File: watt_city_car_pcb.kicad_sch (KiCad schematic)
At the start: 0 parts

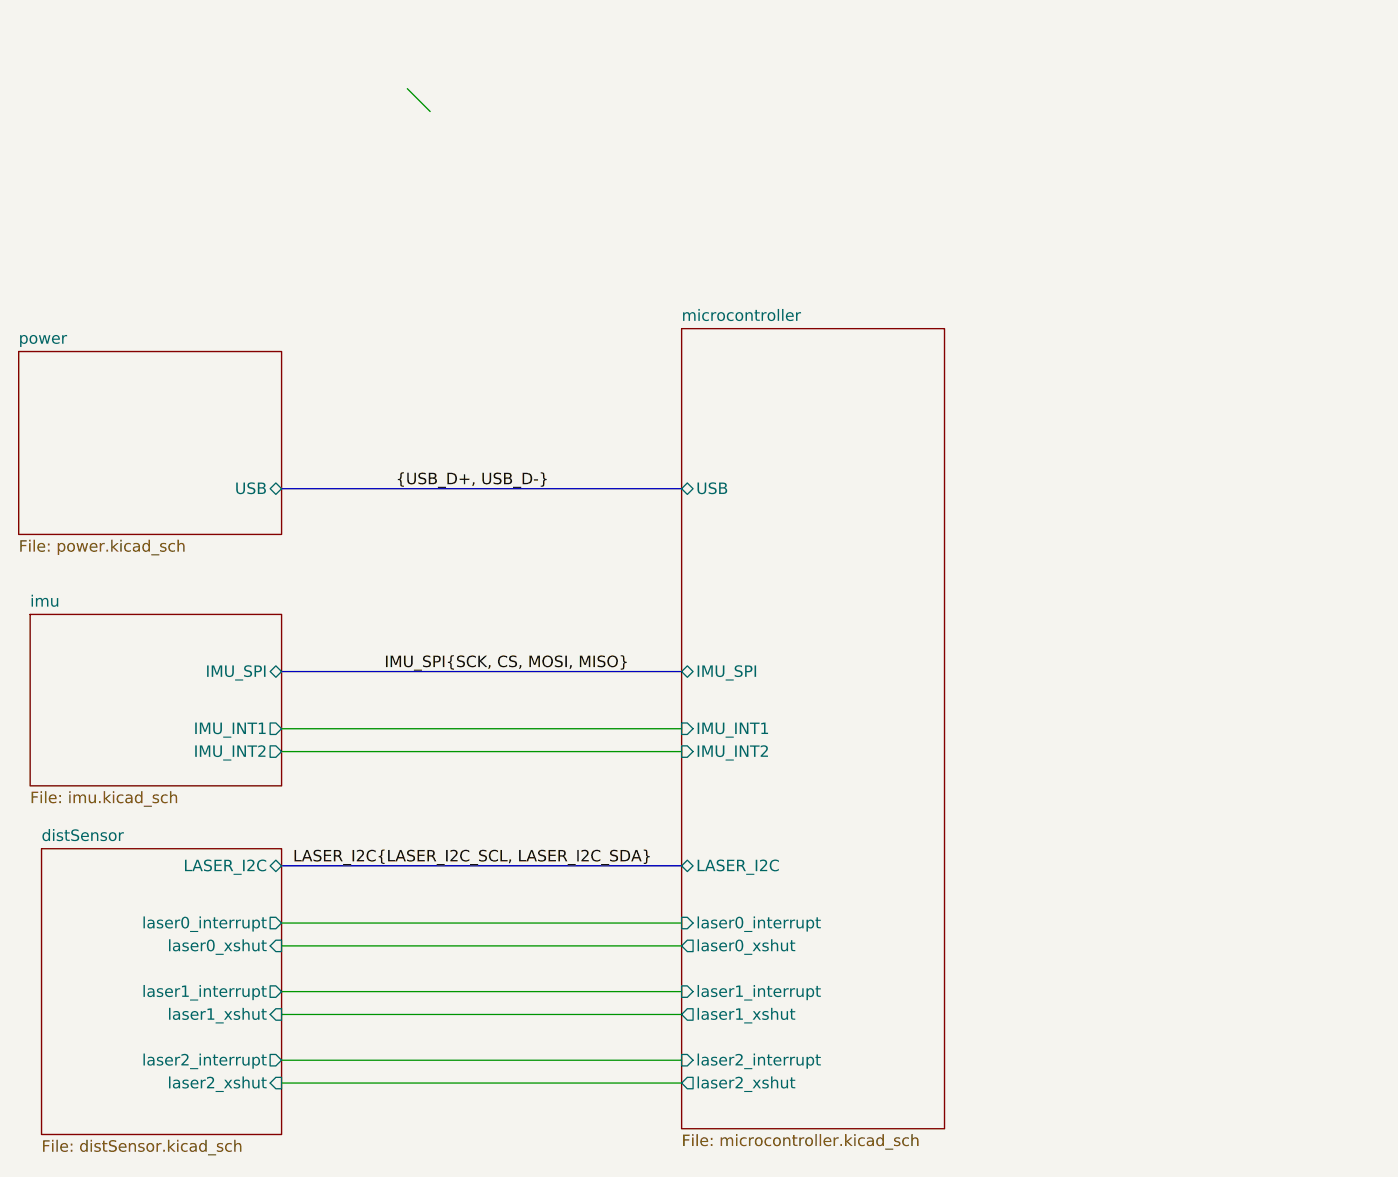
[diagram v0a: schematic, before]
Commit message: added motor controller
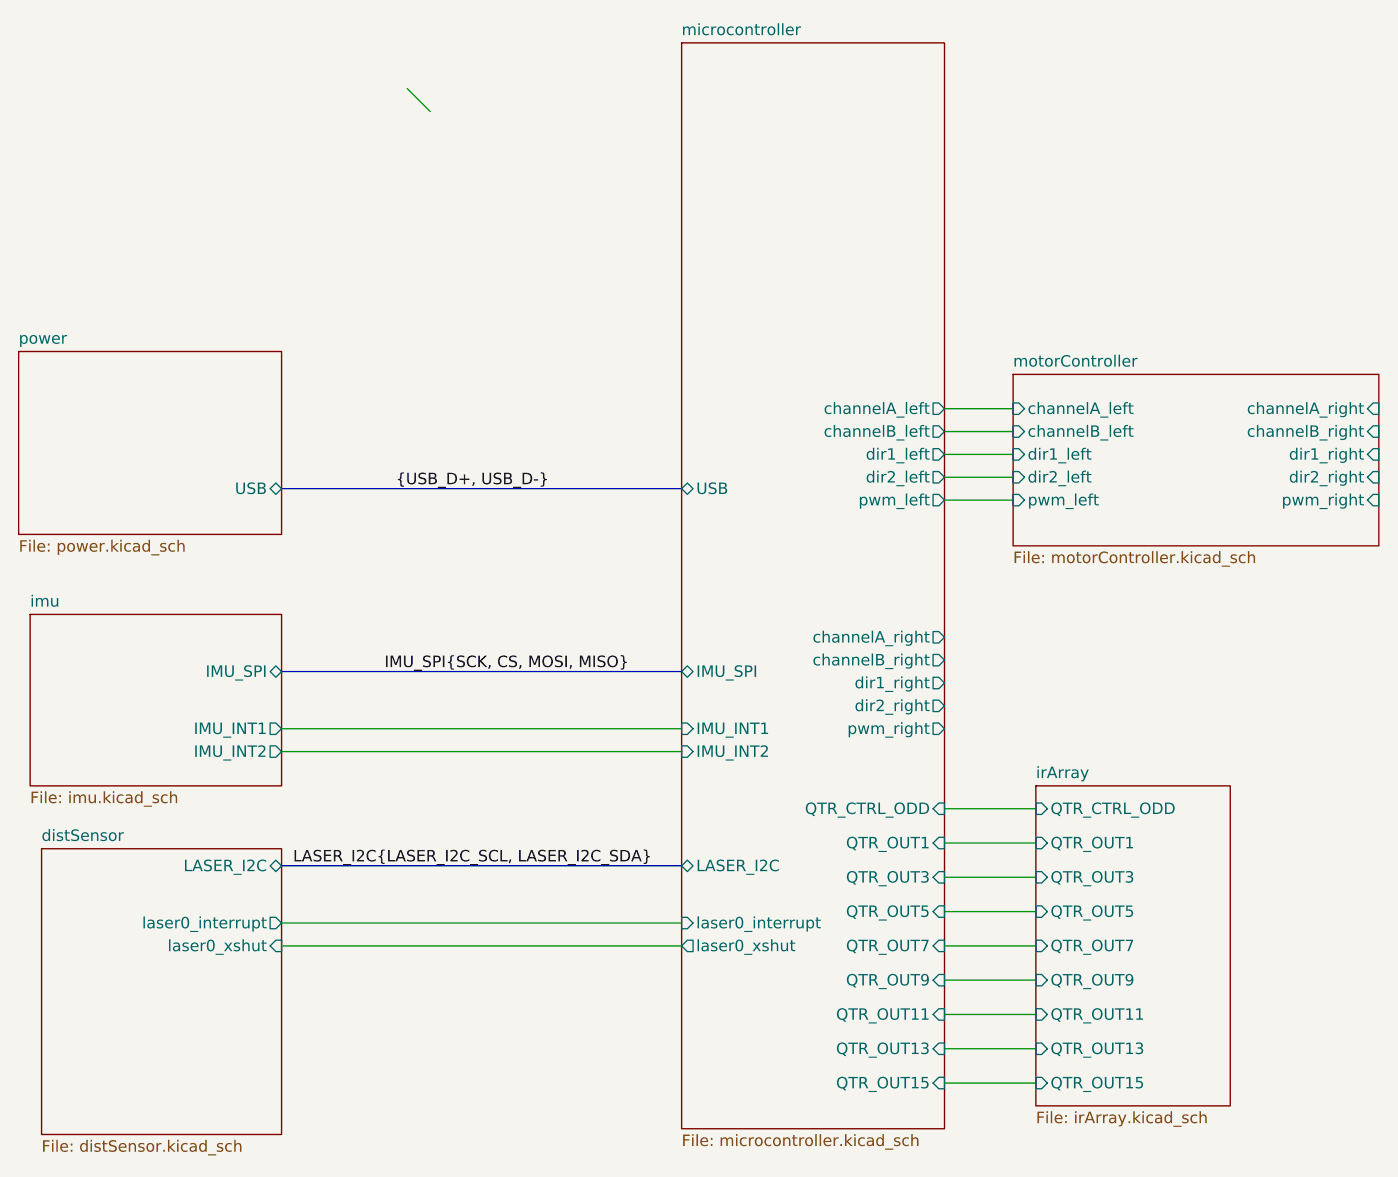
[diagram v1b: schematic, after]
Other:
- added sheet irArray (irArray.kicad_sch)
- added sheet motorController (motorController.kicad_sch)
- sheet distSensor ports: added none; removed laser1_interrupt, laser1_xshut, laser2_interrupt, laser2_xshut
- sheet microcontroller ports: added QTR_CTRL_ODD, QTR_OUT1, QTR_OUT11, QTR_OUT13, QTR_OUT15, QTR_OUT3, QTR_OUT5, QTR_OUT7, QTR_OUT9, channelA_left, channelA_right, channelB_left, channelB_right, dir1_left, dir1_right, dir2_left, dir2_right, pwm_left, pwm_right; removed laser1_interrupt, laser1_xshut, laser2_interrupt, laser2_xshut
